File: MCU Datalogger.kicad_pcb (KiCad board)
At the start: 2 copper layers, 43 x 36.2 mm, 29 parts, among them J1 Conn_01x04_Pin, J2 Conn_01x04_Pin, J3 Conn_01x09_Pin, J4 Conn_02x03_Odd_Even, U1 24LC1025, U2 24LC1025, U3 DS1337S_, U4 ATMEGA328P-AU, Y1 32.768 KHz, Y2 16 MHz

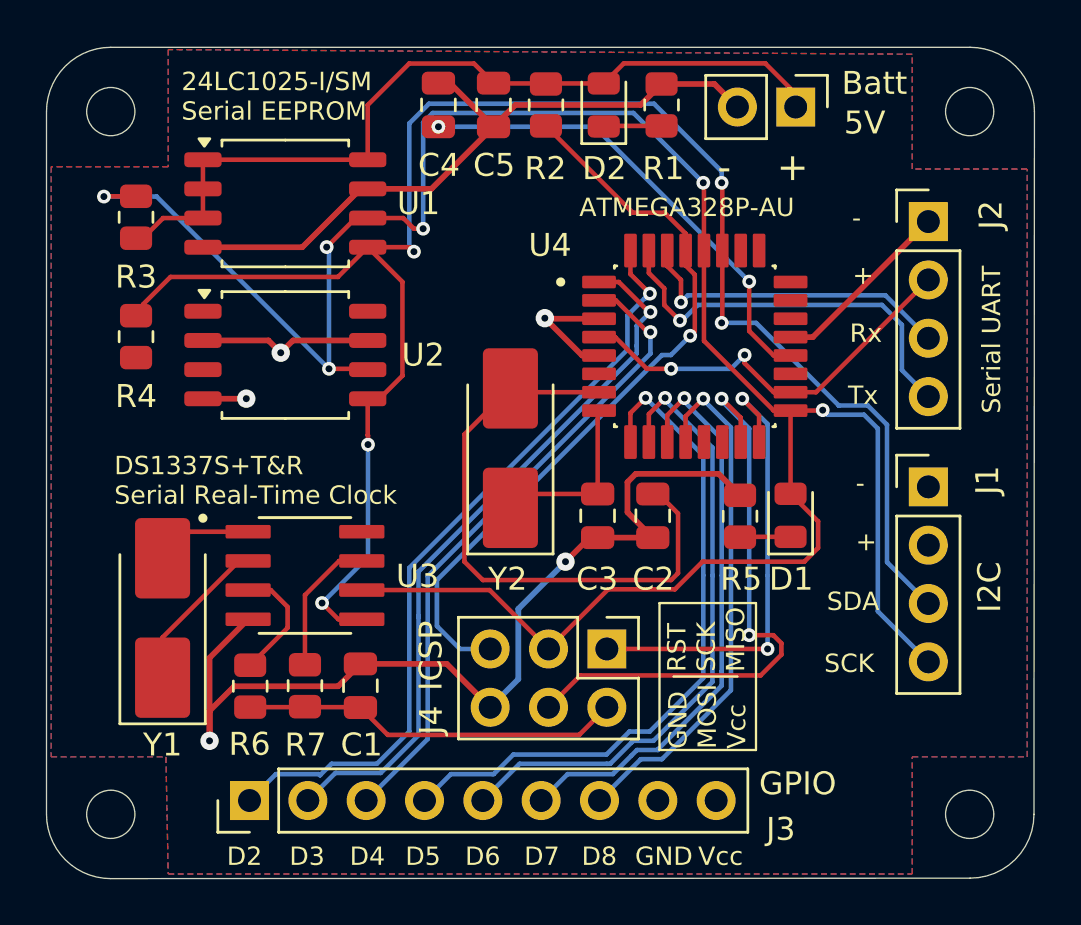
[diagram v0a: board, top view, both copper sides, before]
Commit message: started 2 sided board
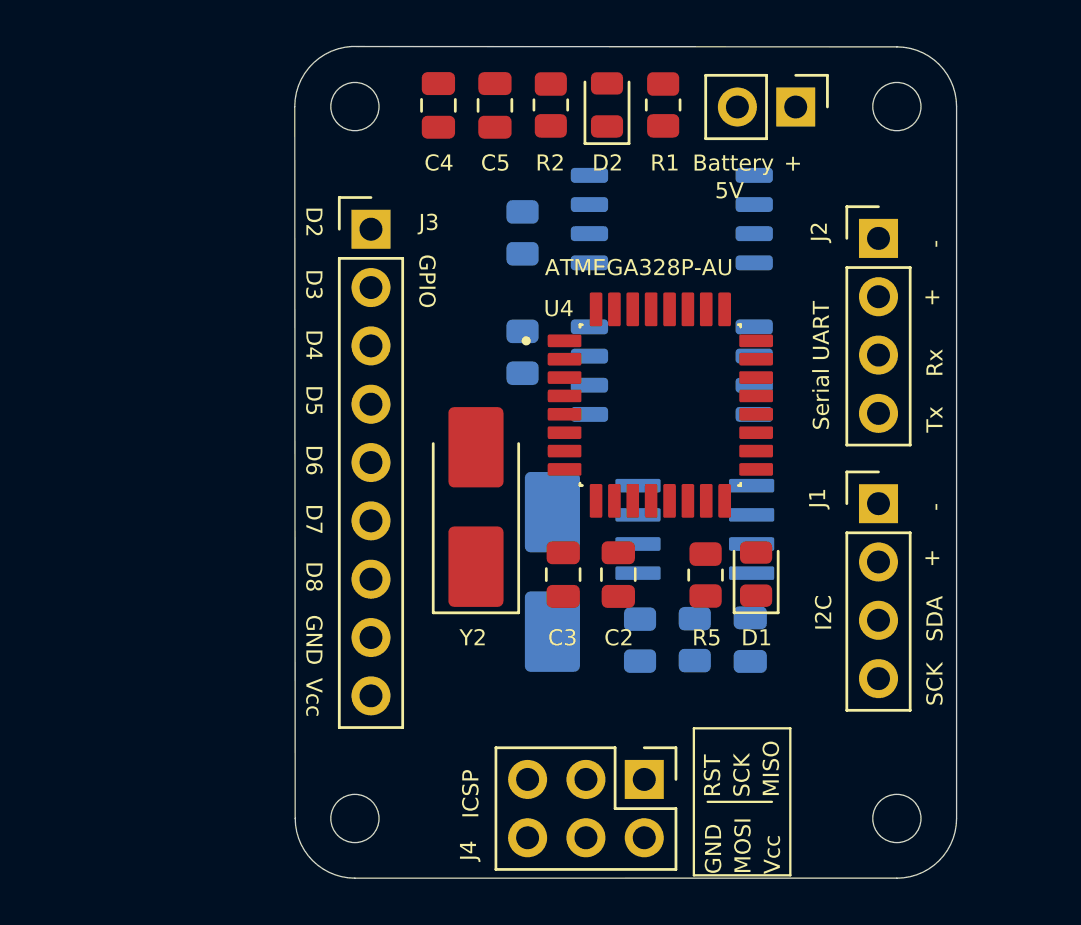
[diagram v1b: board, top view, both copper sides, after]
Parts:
- C1, R3, R4, R6, R7, U1, U2, U3, Y1: moved to B.Cu
- moved J3 25.4 mm to (138.5, 91.7), turned to 0 degrees
- moved C1 17.1 mm to (155.0, 109.6)
- moved R6 17.1 mm to (150.2, 109.6)
- moved R7 17.1 mm to (152.6, 109.6)
- moved Y1 17.1 mm to (146.4, 106.7)
- moved U3 17.1 mm to (152.6, 104.8), turned to 180 degrees
- moved R3 16.8 mm to (145.1, 91.9)
- moved R4 16.8 mm to (145.1, 97.1)
- moved U1 16.8 mm to (151.6, 91.3), turned to 180 degrees
- moved U2 16.8 mm to (151.6, 97.9), turned to 180 degrees
- moved H1 10.6 mm to (137.8, 86.4)
- moved H3 10.6 mm to (137.8, 117.4)
- moved J4 5.91 mm to (150.4, 115.7)
- moved H2 3.18 mm to (161.4, 86.4)
- moved H4 3.18 mm to (161.4, 117.4)
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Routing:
- net /SCK: track 101.7 -> 0.00 mm, vias 6 -> 0
- net GND: track 94.2 -> 0.00 mm, vias 5 -> 0
- net /SDA: track 78.3 -> 0.00 mm, vias 5 -> 0
- net /Vcc: track 71.5 -> 0.00 mm, vias 2 -> 0
- net /D2: track 34.0 -> 0.00 mm, vias 1 -> 0
- net /RESET: track 32.9 -> 0.00 mm, vias 1 -> 0
- net /D3: track 31.4 -> 0.00 mm, vias 1 -> 0
- net /D5: track 29.8 -> 0.00 mm, vias 1 -> 0
- net /D4: track 28.3 -> 0.00 mm, vias 1 -> 0
- net /D6: track 27.6 -> 0.00 mm, vias 1 -> 0
- net Net-(U4-PB6): track 27.0 -> 0.00 mm
- net /MOSI: track 26.3 -> 0.00 mm, vias 2 -> 0
- net /D7: track 25.4 -> 0.00 mm, vias 1 -> 0
- net /D8: track 23.1 -> 0.00 mm, vias 1 -> 0
- net Net-(U4-AREF): track 20.7 -> 0.00 mm, vias 2 -> 0
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- removed copper zone on F.Cu, net /Vcc
- removed copper zone on B.Cu, net GND
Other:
- board size 43 x 36.2 mm -> 28.8 x 36.2 mm
- copper layers 2 -> 4
- board text added: "Battery"
- board text removed: "Batt"

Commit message: route PCB
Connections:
- J1 pad 4: /SCK -> /SCL
- R3 pad 2: /SCK -> /SCL
- U1 pad 6: /SCK -> /SCL
- U2 pad 6: /SCK -> /SCL
- U3 pad 6: /SCK -> /SCL
- U4 pad 28: /SCK -> /SCL
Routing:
- net /Vcc: track 0.00 -> 143.1 mm, vias 0 -> 2
- net GND: track 0.00 -> 115.7 mm, vias 0 -> 4
- net /SCL: track 0.00 -> 55.6 mm, vias 0 -> 2
- net /SDA: track 0.00 -> 52.0 mm, vias 0 -> 3
- net /RESET: track 0.00 -> 37.1 mm, vias 0 -> 1
- net Net-(U4-AREF): track 0.00 -> 27.3 mm, vias 0 -> 2
- net Net-(U4-PB6): track 0.00 -> 21.2 mm
- net Net-(U3-X2): track 0.00 -> 20.3 mm, vias 0 -> 2
- net /MOSI: track 0.00 -> 20.0 mm, vias 0 -> 1
- net /D5: track 0.00 -> 18.7 mm, vias 0 -> 1
- net Net-(U3-X1): track 0.00 -> 18.6 mm, vias 0 -> 2
- net /SCK: track 0.00 -> 17.6 mm
- net /MISO: track 0.00 -> 17.3 mm, vias 0 -> 1
- net /D6: track 0.00 -> 16.5 mm, vias 0 -> 1
- net /D7: track 0.00 -> 16.2 mm, vias 0 -> 1
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- added copper zone on F.Cu, net /Vcc
- added copper zone on B.Cu, net GND
